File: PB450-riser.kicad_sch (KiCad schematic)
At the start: 27 parts, among them J1 J1, J2 J2, P1 PCI 32bit footprint, P2 PCI 32bit footprint (partial)

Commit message: revisions and adding foot prints
revisions and adding footprints
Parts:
- removed J2: J2, symbol Connector:Bus_ISA_16bit
- added J2: J1, Connector:ISA_Mount_Holes, symbol ISA_Mount_Holes:_1
- J1: footprint (none) -> Connector:ISA_Mount_Holes; symbol Connector:Bus_ISA_16bit -> ISA_Mount_Holes:_1
- P1: value PCI 32bit footprint -> ISA Bus over PCI; footprint (none) -> Connector_PCBEdge:BUS_ISA-over-PCI; symbol Connector:Bus_PCI_32bit_5V -> ISA-over-PCI:Bus_ISA_over_PCI_32bit_5V_1
- P2: footprint (none) -> Connector_PCBEdge:BUS_PCI; symbol Connector:Bus_PCI_32bit_5V -> ISA-over-PCI:Bus_ISA_over_PCI_32bit_5V_1
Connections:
- net +12V: now also J1.B9 (+12V), P1.B9 (+12V), J2.B9 (+12V); no longer J1.9 (+12V), P1.B14 (RESERVED)
- net +5: now also P2.A17 (SA14), P2.A29 (SA2), P2.A6 (SD3), P2.B29 (+5V), P2.B4 (IRQ9); no longer P2.A11 (RESERVED), P2.A22 (AD[28]), P2.A35 (GND), P2.B20 (AD[31]), P2.B9 (PRSNT1#)
- net +5V: now also J1.B29 (+5V), J1.B3 (+5V), J1.D16 (+5V), P1.B29 (+5V), P1.B3 (+5V), P1.D16 (+5V), J2.B29 (+5V), J2.B3 (+5V), J2.D16 (+5V); no longer J1.29 (VCC), J1.3 (+5V), J1.78 (+5V), P1.B20 (AD[31]), P1.B59 (+5V), P1.B8 (INTD#)
- net -12V: now also J1.B7 (-12V), P1.B7 (-12V), J2.B7 (-12V); no longer J1.7 (-12V), P1.B12 (GND)
- net -5V: now also J1.B5 (-5V), P1.B5 (-5V), J2.B5 (-5V); no longer J1.5 (-5V), P1.B10 (RESERVED)
- net GND: now also J1.B1 (GND), J1.B10 (GND), J1.B31 (GND), J1.D18 (GND), P1.A1' (GND), P1.A22' (GND), P1.B1 (GND), P1.B1' (GND), P1.B10 (GND), P1.B31 (GND), P1.C18' (GND), P1.C8' (GND), P1.D18 (GND), P1.D18' (GND), P2.A15 (SA16), P2.A24 (SA7), P2.A4 (SD5), P2.B1 (GND), P2.B16 (DRQ3), P2.B9 (+12V), J2.B1 (GND), J2.B10 (GND), J2.B31 (GND), J2.D18 (GND); no longer J1.1 (GND), J1.10 (GND), J1.31 (GND), J1.80 (GND), P1.A28 (AD[22]), P1.A48 (GND), P1.A5 (+5V), P1.A62 (+5V), P1.B25 (+3.3V), P1.B40 (PERR#), P1.B5 (+5V), P1.B6 (+5V), P1.B61 (+5V), P1.B62 (+5V), P2.A20 (AD[30]), P2.A3 (TMS), P2.A30 (GND), P2.A38 (STOP#), P2.A9 (RESERVED), P2.B14 (RESERVED), P2.B29 (AD[21]), P2.B38 (GND), P2.B6 (+5V)
- net VCC: now also P2.B25 (IRQ3); no longer C2.1, P2.B32 (AD[17])
- net at P1.A1 (IO_CH_CK): now also J1.A1 (~{IO_CH_CK}), J2.A1 (~{IO_CH_CK})
- net at P1.A10 (IO_CH_RDY): now also J1.A10 (IO_CH_RDY), J2.A10 (IO_CH_RDY)
- net at P1.A11 (AEN): now also J1.A11 (AEN), J2.A11 (AEN)
- net SA19: now reaches P1.A12 (SA19)
- net SA19: now also J1.A12 (SA19), J2.A12 (SA19)
- net SA18: now reaches P1.A13 (SA18)
- net SA18: now also J1.A13 (SA18), J2.A13 (SA18)
- net SA17: now reaches P1.A14 (SA17)
- net SA17: now also J1.A14 (SA17), J2.A14 (SA17)
- net SA16: now reaches P1.A15 (SA16)
- net SA16: now also J1.A15 (SA16), J2.A15 (SA16); no longer J1.41 (IO_READY)
- net SA15: now reaches P1.A16 (SA15)
- net SA15: now also J1.A16 (SA15), J2.A16 (SA15); no longer J1.42 (AEN)
- net SA14: now reaches P1.A17 (SA14)
- net SA14: now also J1.A17 (SA14), J2.A17 (SA14)
- net SA13: now reaches P1.A18 (SA13)
- net SA13: now also J1.A18 (SA13), J2.A18 (SA13)
- net SA12: now reaches P1.A19 (SA12)
- net SA12: now also J1.A19 (SA12), J2.A19 (SA12)
- net SD7: now reaches P1.A2 (SD7)
- net SD7: now also J1.A2 (SD7), J2.A2 (SD7)
- net SA11: now reaches P1.A20 (SA11)
- net SA11: now also J1.A20 (SA11), J2.A20 (SA11)
- net SA10: now reaches P1.A21 (SA10)
- net SA10: now also J1.A21 (SA10), J2.A21 (SA10)
- net SA9: now reaches P1.A22 (SA9)
- net SA9: now also J1.A22 (SA9), J2.A22 (SA9)
- net SA8: now reaches P1.A23 (SA8)
- net SA8: now also J1.A23 (SA8), J2.A23 (SA8)
- net SA7: now reaches P1.A24 (SA7)
- net SA7: now also J1.A24 (SA7), J2.A24 (SA7)
- net SA6: now reaches P1.A25 (SA6)
- net SA6: now also J1.A25 (SA6), J2.A25 (SA6)
- net SA5: now reaches P1.A26 (SA5)
- net SA5: now also J1.A26 (SA5), J2.A26 (SA5)
- net SA4: now reaches P1.A27 (SA4)
- net SA4: now also J1.A27 (SA4), J2.A27 (SA4)
- net SA2: now reaches P1.A29 (SA2)
- net SA2: now also J1.A29 (SA2), J2.A29 (SA2)
- net SD6: now reaches P1.A3 (SD6)
- net SD6: now also J1.A3 (SD6), J2.A3 (SD6)
- net SA1: now reaches P1.A30 (SA1)
- net SA1: now also J1.A30 (SA1), J2.A30 (SA1)
- net SA0: now reaches P1.A31 (SA0)
- net SA0: now also J1.A31 (SA0), J2.A31 (SA0)
- net SD5: now reaches P1.A4 (SD5)
- net SD5: now also J1.A4 (SD5), J2.A4 (SD5)
- net SD3: now reaches P1.A6 (SD3)
- net SD3: now also J1.A6 (SD3), J2.A6 (SD3); no longer J1.32 (IO)
- net SD2: now reaches P1.A7 (SD2)
- net SD2: now also J1.A7 (SD2), J2.A7 (SD2)
- net SD1: now reaches P1.A8 (SD1)
- net SD1: now also J1.A8 (SD1), J2.A8 (SD1)
- net SD0: now reaches P1.A9 (SD0)
- net SD0: now also J1.A9 (SD0), J2.A9 (SD0)
- net at P1.B11 (~{SMEMW}): now also J1.B11 (~{SMEMW}), J2.B11 (~{SMEMW}); no longer J1.6 (DRQ2)
- net at P1.B13 (~{IOW}): now also J1.B13 (~{IOW}), J2.B13 (~{IOW}); no longer J1.8 (UNUSED)
- net at P1.B15 (~{DACK3}): now also J1.B15 (~{DACK3}), J2.B15 (~{DACK3})
- net at P1.B16 (DRQ3): now also J1.B16 (DRQ3), J2.B16 (DRQ3); no longer J1.11 (~{SMEMW})
- net at P1.B17 (~{DACK1}): now also J1.B17 (~{DACK1}), J2.B17 (~{DACK1}); no longer J1.12 (~{SMEMR})
- net at P1.B18 (DRQ1): now also J1.B18 (DRQ1), J2.B18 (DRQ1); no longer J1.13 (~{IOW})
- net at P1.B2 (RESETDRV): now also J1.B2 (RESETDRV), J2.B2 (RESETDRV)
- net at P1.B21 (IRQ7): now also J1.B20 (SYSCLK), J2.B20 (SYSCLK); no longer J1.15 (~{DACK3})
- net at P1.B22 (IRQ6): now also J1.B21 (IRQ7), J2.B21 (IRQ7); no longer J1.16 (DRQ3)
- net at P1.B23 (IRQ5): now also J1.B22 (IRQ6), J2.B22 (IRQ6); no longer J1.17 (~{DACK1})
- net at P1.B24 (IRQ4): now also J1.B23 (IRQ5), J2.B23 (IRQ5); no longer J1.18 (DRQ1)
- net at P1.B26 (~{DACK2}): now also J1.B25 (IRQ3), J2.B25 (IRQ3); no longer J1.19 (~{REFRESH})
- net at P1.B27 (TC): now also J1.B26 (~{DACK2}), J2.B26 (~{DACK2}); no longer J1.20 (CLK)
- net at P1.B28 (BALE): now also J1.B27 (TC), J2.B27 (TC)
- net at P1.B30 (OSC): now also J1.B30 (OSC), J2.B30 (OSC); no longer J1.22 (IRQ6)
- net at P1.B4 (IRQ9): now also J1.B4 (IRQ9), J2.B4 (IRQ9)
- new net: J1.B12 (~{SMEMR}), J2.B12 (~{SMEMR}), P1.B12 (~{SMEMR})
- new net: J1.B14 (~{IOR}), J2.B14 (~{IOR}), P1.B14 (~{IOR})
- new net: J1.B19 (~{REFRESH}), J2.B19 (~{REFRESH}), P1.B20 (SYSCLK)
- new net: J1.B24 (IRQ4), J2.B24 (IRQ4), P1.B25 (IRQ3)
- new net: J1.B28 (BALE), J2.B28 (BALE), P1.B29 (+5V)
- new net: J1.B6 (DRQ2), J2.B6 (DRQ2), P1.B6 (DRQ2)
- new net: J1.B8 (~{0WS}), J2.B8 (~{0WS}), P1.B8 (~{0WS})
- new net: J1.C1 (SBHE), J2.C1 (SBHE), P1.C1 (SBHE)
- new net: J1.C10 (~{MEMW}), J2.C10 (~{MEMW}), P1.C10 (~{MEMW})
- new net: J1.C9 (~{MEMR}), J2.C9 (~{MEMR}), P1.C9 (~{MEMR})
- new net: J1.D1 (~{MEMCS16}), J2.D1 (~{MEMCS16}), P1.D1 (~{MEMCS16})
- new net: J1.D10 (~{DACK5}), J2.D10 (~{DACK5}), P1.D10 (~{DACK5})
- new net: J1.D11 (DRQ5), J2.D11 (DRQ5), P1.D11 (DRQ5)
- new net: J1.D12 (~{DACK6}), J2.D12 (~{DACK6}), P1.D12 (~{DACK6})
- new net: J1.D13 (DRQ6), J2.D13 (DRQ6), P1.D13 (DRQ6)
- new net: J1.D14 (~{DACK7}), J2.D14 (~{DACK7}), P1.D14 (~{DACK7})
- new net: J1.D15 (DRQ7), J2.D15 (DRQ7), P1.D15 (DRQ7)
- new net: J1.D17 (~{MASTER}), J2.D17 (~{MASTER}), P1.D17 (~{MASTER})
- new net: J1.D2 (~{IOCS16}), J2.D2 (~{IOCS16}), P1.D2 (~{IOCS16})
- new net: J1.D3 (IRQ10), J2.D3 (IRQ10), P1.D3 (IRQ10)
- new net: J1.D4 (IRQ11), J2.D4 (IRQ11), P1.D4 (IRQ11)
- new net: J1.D5 (IRQ12), J2.D5 (IRQ12), P1.D5 (IRQ12)
- new net: J1.D6 (IRQ15), J2.D6 (IRQ15), P1.D6 (IRQ15)
- new net: J1.D7 (IRQ14), J2.D7 (IRQ14), P1.D7 (IRQ14)
- new net: J1.D8 (~{DACK0}), J2.D8 (~{DACK0}), P1.D8 (~{DACK0))
- new net: J1.D9 (DRQ0), J2.D9 (DRQ0), P1.D9 (DRQ0)
- new net LA17: J1.C8 (LA17), J2.C8 (LA17), P1.C8 (LA17)
- new net LA18: J1.C7 (LA18), J2.C7 (LA18), P1.C7 (LA18)
- new net LA19: J1.C6 (LA19), J2.C6 (LA19), P1.C6 (LA19)
- new net LA20: J1.C5 (LA20), J2.C5 (LA20), P1.C5 (LA20)
- new net LA21: J1.C4 (LA21), J2.C4 (LA21), P1.C4 (LA21)
- new net LA22: J1.C3 (LA22), J2.C3 (LA22), P1.C3 (LA22)
- new net LA23: J1.C2 (LA23), J2.C2 (LA23), P1.C2 (LA23)
- new net SA3: J1.A28 (SA3), J2.A28 (SA3), P1.A28 (SA3)
- new net SD10: J1.C13 (SD10), J2.C13 (SD10), P1.C13 (SD10)
- new net SD11: J1.C14 (SD11), J2.C14 (SD11), P1.C14 (SD11)
- new net SD12: J1.C15 (SD12), J2.C15 (SD12), P1.C15 (SD12)
- new net SD13: J1.C16 (SD13), J2.C16 (SD13), P1.C16 (SD13)
- new net SD14: J1.C17 (SD14), J2.C17 (SD14), P1.C17 (SD14)
- new net SD15: J1.C18 (SD15), J2.C18 (SD15), P1.C18 (SD15)
- new net SD4: J1.A5 (SD4), J2.A5 (SD4), P1.A5 (SD4)
- new net SD8: J1.C11 (SD8), J2.C11 (SD8), P1.C11 (SD8)
- new net SD9: J1.C12 (SD9), J2.C12 (SD9), P1.C12 (SD9)
- no-connect marks 77 -> 62
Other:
- moved on the sheet: J1

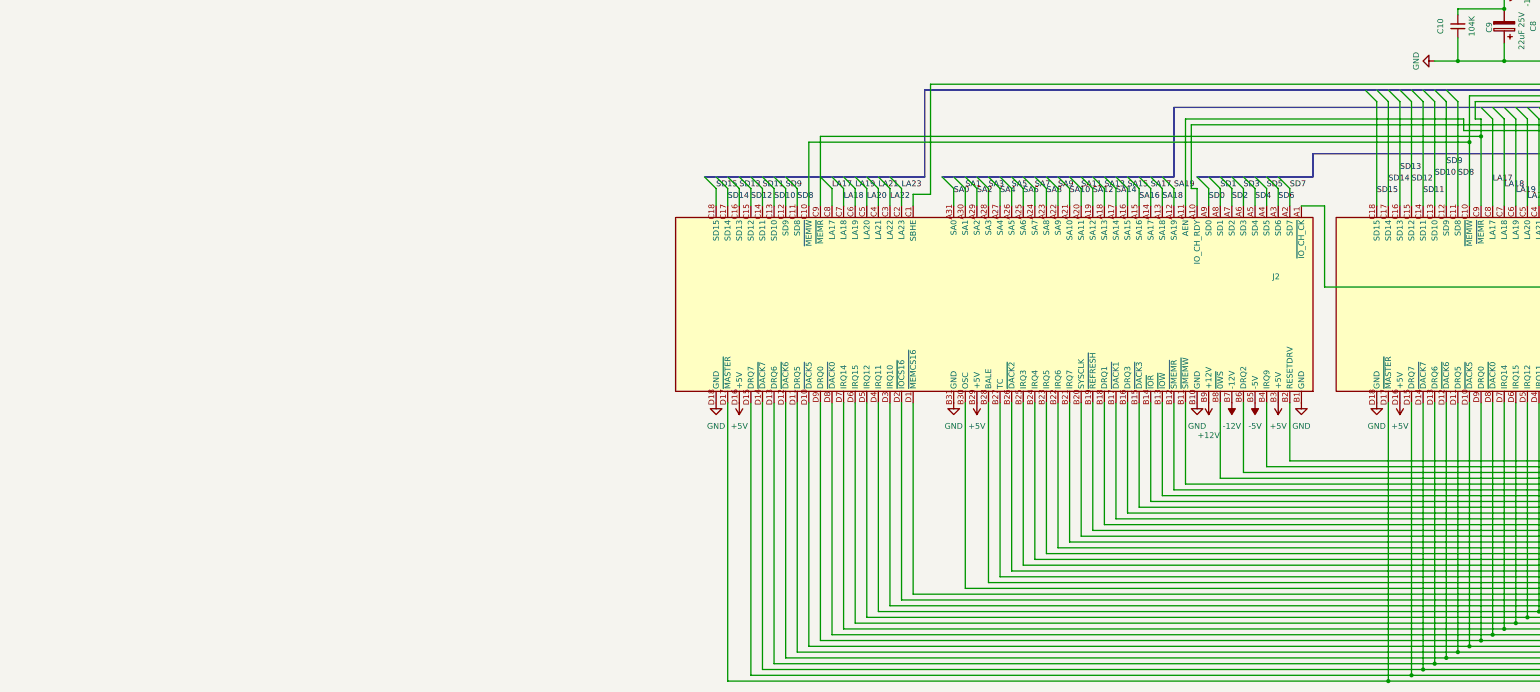
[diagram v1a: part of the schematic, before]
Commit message: added third slot and gerber files
added third slot and gerber files
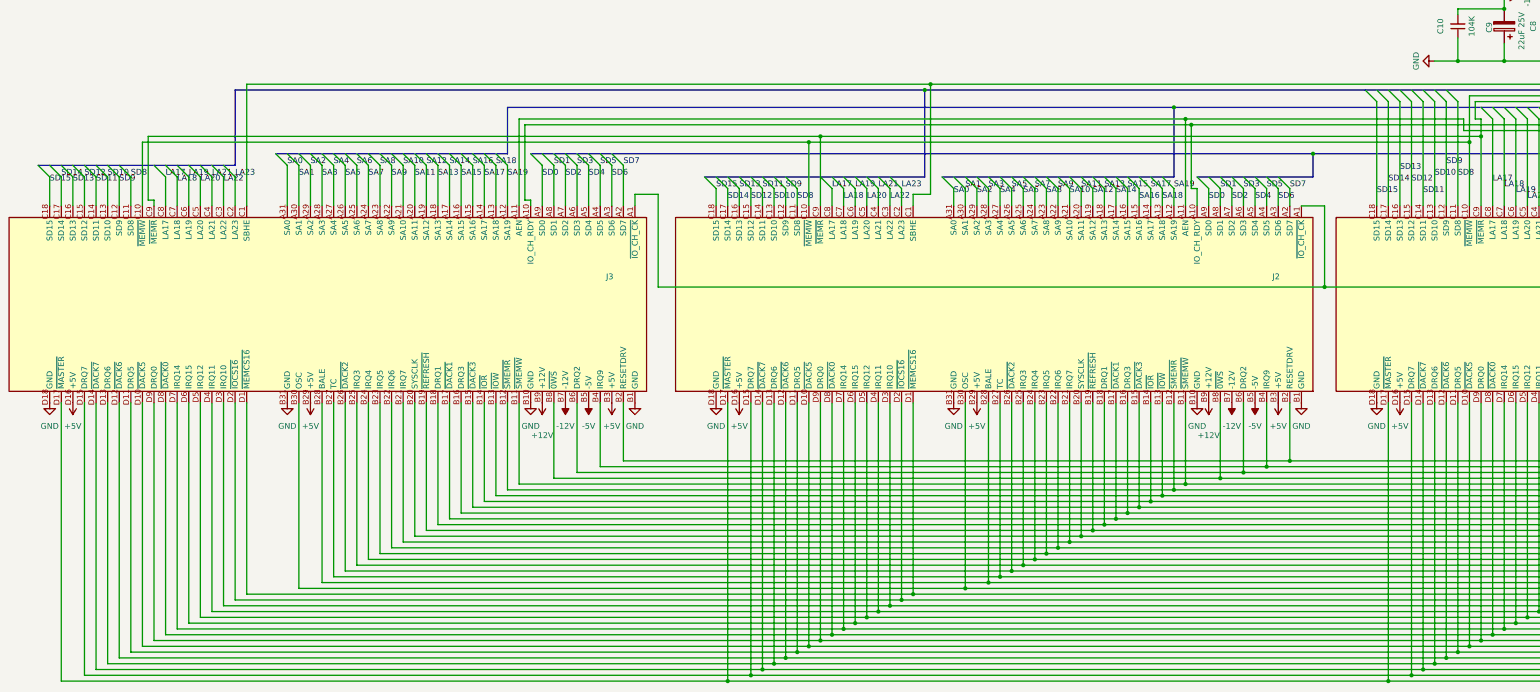
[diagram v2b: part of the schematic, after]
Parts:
- added J3: J1, Connector:ISA_Mount_Holes, symbol ISA_Mount_Holes:_1
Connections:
- net +12V: now also J3.B9 (+12V)
- net +5V: now also J3.B29 (+5V), J3.B3 (+5V), J3.D16 (+5V)
- net -12V: now also J3.B7 (-12V)
- net -5V: now also J3.B5 (-5V)
- net GND: now also J3.B1 (GND), J3.B10 (GND), J3.B31 (GND), J3.D18 (GND)
- net LA17: now also J3.C8 (LA17)
- net LA18: now also J3.C7 (LA18)
- net LA19: now also J3.C6 (LA19)
- net LA20: now also J3.C5 (LA20)
- net LA21: now also J3.C4 (LA21)
- net LA22: now also J3.C3 (LA22)
- net LA23: now also J3.C2 (LA23)
- net SA0: now also J3.A31 (SA0)
- net SA1: now also J3.A30 (SA1)
- net SA10: now also J3.A21 (SA10)
- net SA11: now also J3.A20 (SA11)
- net SA12: now also J3.A19 (SA12)
- net SA13: now also J3.A18 (SA13)
- net SA14: now also J3.A17 (SA14)
- net SA15: now also J3.A16 (SA15)
- net SA16: now also J3.A15 (SA16)
- net SA17: now also J3.A14 (SA17)
- net SA18: now also J3.A13 (SA18)
- net SA19: now also J3.A12 (SA19)
- net SA2: now also J3.A29 (SA2)
- net SA3: now also J3.A28 (SA3)
- net SA4: now also J3.A27 (SA4)
- net SA5: now also J3.A26 (SA5)
- net SA6: now also J3.A25 (SA6)
- net SA7: now also J3.A24 (SA7)
- net SA8: now also J3.A23 (SA8)
- net SA9: now also J3.A22 (SA9)
- net SD0: now also J3.A9 (SD0)
- net SD1: now also J3.A8 (SD1)
- net SD10: now also J3.C13 (SD10)
- net SD11: now also J3.C14 (SD11)
- net SD12: now also J3.C15 (SD12)
- net SD13: now also J3.C16 (SD13)
- net SD14: now also J3.C17 (SD14)
- net SD15: now also J3.C18 (SD15)
- net SD2: now also J3.A7 (SD2)
- net SD3: now also J3.A6 (SD3)
- net SD4: now also J3.A5 (SD4)
- net SD5: now also J3.A4 (SD5)
- net SD6: now also J3.A3 (SD6)
- net SD7: now also J3.A2 (SD7)
- net SD8: now also J3.C11 (SD8)
- net SD9: now also J3.C12 (SD9)
- net at J1.A1 (~{IO_CH_CK}), J2.A1 (~{IO_CH_CK}), P1.A1 (IO_CH_CK): now also J3.A1 (~{IO_CH_CK})
- net at J1.A10 (IO_CH_RDY), J2.A10 (IO_CH_RDY), P1.A10 (IO_CH_RDY): now also J3.A10 (IO_CH_RDY)
- net at J1.A11 (AEN), J2.A11 (AEN), P1.A11 (AEN): now also J3.A11 (AEN)
- net at J1.B11 (~{SMEMW}), J2.B11 (~{SMEMW}), P1.B11 (~{SMEMW}): now also J3.B11 (~{SMEMW})
- net at J1.B12 (~{SMEMR}), J2.B12 (~{SMEMR}), P1.B12 (~{SMEMR}): now also J3.B12 (~{SMEMR})
- net at J1.B13 (~{IOW}), J2.B13 (~{IOW}), P1.B13 (~{IOW}): now also J3.B13 (~{IOW})
- net at J1.B14 (~{IOR}), J2.B14 (~{IOR}), P1.B14 (~{IOR}): now also J3.B14 (~{IOR})
- net at J1.B15 (~{DACK3}), J2.B15 (~{DACK3}), P1.B15 (~{DACK3}): now also J3.B15 (~{DACK3})
- net at J1.B16 (DRQ3), J2.B16 (DRQ3), P1.B16 (DRQ3): now also J3.B16 (DRQ3)
- net at J1.B17 (~{DACK1}), J2.B17 (~{DACK1}), P1.B17 (~{DACK1}): now also J3.B17 (~{DACK1})
- net at J1.B18 (DRQ1), J2.B18 (DRQ1), P1.B18 (DRQ1): now also J3.B18 (DRQ1)
- net at J1.B2 (RESETDRV), J2.B2 (RESETDRV), P1.B2 (RESETDRV): now also J3.B2 (RESETDRV)
- net at J1.B19 (~{REFRESH}), J2.B19 (~{REFRESH}), P1.B20 (SYSCLK): now also J3.B19 (~{REFRESH})
- net at J1.B20 (SYSCLK), J2.B20 (SYSCLK), P1.B21 (IRQ7): now also J3.B20 (SYSCLK)
- net at J1.B21 (IRQ7), J2.B21 (IRQ7), P1.B22 (IRQ6): now also J3.B21 (IRQ7)
- net at J1.B22 (IRQ6), J2.B22 (IRQ6), P1.B23 (IRQ5): now also J3.B22 (IRQ6)
- net at J1.B23 (IRQ5), J2.B23 (IRQ5), P1.B24 (IRQ4): now also J3.B23 (IRQ5)
- net at J1.B24 (IRQ4), J2.B24 (IRQ4), P1.B25 (IRQ3): now also J3.B24 (IRQ4)
- net at J1.B25 (IRQ3), J2.B25 (IRQ3), P1.B26 (~{DACK2}): now also J3.B25 (IRQ3)
- net at J1.B26 (~{DACK2}), J2.B26 (~{DACK2}), P1.B27 (TC): now also J3.B26 (~{DACK2})
- net at J1.B27 (TC), J2.B27 (TC), P1.B28 (BALE): now also J3.B27 (TC)
- net at J1.B28 (BALE), J2.B28 (BALE), P1.B29 (+5V): now also J3.B28 (BALE)
- net at J1.B30 (OSC), J2.B30 (OSC), P1.B30 (OSC): now also J3.B30 (OSC)
- net at J1.B4 (IRQ9), J2.B4 (IRQ9), P1.B4 (IRQ9): now also J3.B4 (IRQ9)
- net at J1.B6 (DRQ2), J2.B6 (DRQ2), P1.B6 (DRQ2): now also J3.B6 (DRQ2)
- net at J1.B8 (~{0WS}), J2.B8 (~{0WS}), P1.B8 (~{0WS}): now also J3.B8 (~{0WS})
- net at J1.C1 (SBHE), J2.C1 (SBHE), P1.C1 (SBHE): now also J3.C1 (SBHE)
- net at J1.C10 (~{MEMW}), J2.C10 (~{MEMW}), P1.C10 (~{MEMW}): now also J3.C10 (~{MEMW})
- net at J1.C9 (~{MEMR}), J2.C9 (~{MEMR}), P1.C9 (~{MEMR}): now also J3.C9 (~{MEMR})
- net at J1.D1 (~{MEMCS16}), J2.D1 (~{MEMCS16}), P1.D1 (~{MEMCS16}): now also J3.D1 (~{MEMCS16})
- net at J1.D10 (~{DACK5}), J2.D10 (~{DACK5}), P1.D10 (~{DACK5}): now also J3.D10 (~{DACK5})
- net at J1.D11 (DRQ5), J2.D11 (DRQ5), P1.D11 (DRQ5): now also J3.D11 (DRQ5)
- net at J1.D12 (~{DACK6}), J2.D12 (~{DACK6}), P1.D12 (~{DACK6}): now also J3.D12 (~{DACK6})
- net at J1.D13 (DRQ6), J2.D13 (DRQ6), P1.D13 (DRQ6): now also J3.D13 (DRQ6)
- net at J1.D14 (~{DACK7}), J2.D14 (~{DACK7}), P1.D14 (~{DACK7}): now also J3.D14 (~{DACK7})
- net at J1.D15 (DRQ7), J2.D15 (DRQ7), P1.D15 (DRQ7): now also J3.D15 (DRQ7)
- net at J1.D17 (~{MASTER}), J2.D17 (~{MASTER}), P1.D17 (~{MASTER}): now also J3.D17 (~{MASTER})
- net at J1.D2 (~{IOCS16}), J2.D2 (~{IOCS16}), P1.D2 (~{IOCS16}): now also J3.D2 (~{IOCS16})
- net at J1.D3 (IRQ10), J2.D3 (IRQ10), P1.D3 (IRQ10): now also J3.D3 (IRQ10)
- net at J1.D4 (IRQ11), J2.D4 (IRQ11), P1.D4 (IRQ11): now also J3.D4 (IRQ11)
- net at J1.D5 (IRQ12), J2.D5 (IRQ12), P1.D5 (IRQ12): now also J3.D5 (IRQ12)
- net at J1.D6 (IRQ15), J2.D6 (IRQ15), P1.D6 (IRQ15): now also J3.D6 (IRQ15)
- net at J1.D7 (IRQ14), J2.D7 (IRQ14), P1.D7 (IRQ14): now also J3.D7 (IRQ14)
- net at J1.D8 (~{DACK0}), J2.D8 (~{DACK0}), P1.D8 (~{DACK0)): now also J3.D8 (~{DACK0})
- net at J1.D9 (DRQ0), J2.D9 (DRQ0), P1.D9 (DRQ0): now also J3.D9 (DRQ0)

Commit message: Added capacitors and trace optimization
Added capacitors and trace optimization
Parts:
- C1, C11, C17, C18, C2, C20, C21, C7, C9: footprint (none) -> Capacitor_THT:CP_Radial_D5.0mm_P2.00mm
- C10, C12, C13, C14, C15, C16, C19, C22, C23, C3, C4, C5, C6, C8: footprint (none) -> Capacitor_THT:C_Disc_D5.0mm_W2.5mm_P2.50mm
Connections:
- net +5V: now also C1.1, C11.1, C12.1, C13.2, C14.2, C15.2, C16.2, C17.1, C18.1, C19.2, C2.1, C20.1, C21.1, C22.2, C23.2, C3.2, C4.2, C5.2, C6.2
- net GND: now also C12.2; no longer C12.1
- net VCC: no longer C1.1, C11.1, C12.2, C13.2, C14.2, C15.2, C16.2, C17.1, C18.1, C19.2, C20.1, C21.1, C22.2, C23.2, C3.2, C4.2, C5.2, C6.2
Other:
- moved on the sheet: C12, C13, C14, C15, C16, C19, C22, C23

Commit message: Fixed small bug in PCI footprint
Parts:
- P1: footprint Connector_PCBEdge:BUS_ISA-over-PCI -> Connector_PCBEdge:BUS_PCI
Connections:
- net +12V: now also C11.2, C12.1
- net +5V: no longer C11.1, C12.1
- net GND: now also C11.1; no longer C11.2
- net /IO_CH_CLK: now reaches J1.A1 (~{IO_CH_CK}), J2.A1 (~{IO_CH_CK}), J3.A1 (~{IO_CH_CK}), P1.A1 (IO_CH_CK)
- net IO_CH_RDY: now reaches J1.A10 (IO_CH_RDY), J2.A10 (IO_CH_RDY), J3.A10 (IO_CH_RDY), P1.A10 (IO_CH_RDY)
- net AEN: now reaches J1.A11 (AEN), J2.A11 (AEN), J3.A11 (AEN), P1.A11 (AEN)
- net at J1.B19 (~{REFRESH}), J2.B19 (~{REFRESH}), J3.B19 (~{REFRESH}): now also P1.B19 (REFRESH); no longer P1.B20 (SYSCLK)
- net at J1.B20 (SYSCLK), J2.B20 (SYSCLK), J3.B20 (SYSCLK): now also P1.B20 (SYSCLK); no longer P1.B21 (IRQ7)
- net at J1.B21 (IRQ7), J2.B21 (IRQ7), J3.B21 (IRQ7): now also P1.B21 (IRQ7); no longer P1.B22 (IRQ6)
- net at J1.B22 (IRQ6), J2.B22 (IRQ6), J3.B22 (IRQ6): now also P1.B22 (IRQ6); no longer P1.B23 (IRQ5)
- net at J1.B23 (IRQ5), J2.B23 (IRQ5), J3.B23 (IRQ5): now also P1.B23 (IRQ5); no longer P1.B24 (IRQ4)
- net at J1.B24 (IRQ4), J2.B24 (IRQ4), J3.B24 (IRQ4): now also P1.B24 (IRQ4); no longer P1.B25 (IRQ3)
- net at J1.B25 (IRQ3), J2.B25 (IRQ3), J3.B25 (IRQ3): now also P1.B25 (IRQ3); no longer P1.B26 (~{DACK2})
- net at J1.B26 (~{DACK2}), J2.B26 (~{DACK2}), J3.B26 (~{DACK2}): now also P1.B26 (~{DACK2}); no longer P1.B27 (TC)
- net at J1.B27 (TC), J2.B27 (TC), J3.B27 (TC): now also P1.B27 (TC); no longer P1.B28 (BALE)
- net at J1.B28 (BALE), J2.B28 (BALE), J3.B28 (BALE): now also P1.B28 (BALE); no longer P1.B29 (+5V)
- net SBHE: now reaches J1.C1 (SBHE), J2.C1 (SBHE), J3.C1 (SBHE), P1.C1 (SBHE)
- net /MEMW: now reaches J1.C10 (~{MEMW}), J2.C10 (~{MEMW}), J3.C10 (~{MEMW}), P1.C10 (~{MEMW})
- net /MEMR: now reaches J1.C9 (~{MEMR}), J2.C9 (~{MEMR}), J3.C9 (~{MEMR}), P1.C9 (~{MEMR})
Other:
- moved on the sheet: J1, P2
